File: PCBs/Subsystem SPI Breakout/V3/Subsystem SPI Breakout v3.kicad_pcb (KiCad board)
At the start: 2 copper layers, 91.4 x 53.3 mm, 33 parts

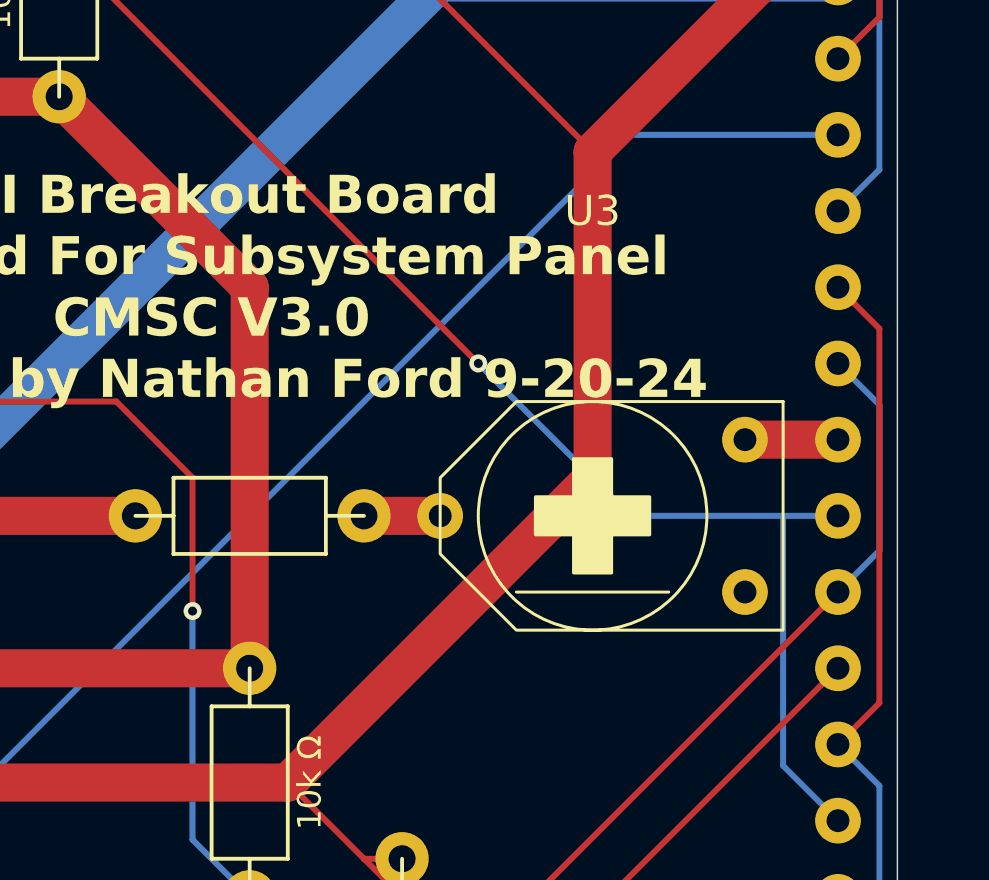
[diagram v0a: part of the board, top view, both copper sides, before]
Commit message: Fixed some labels on the silkscreen
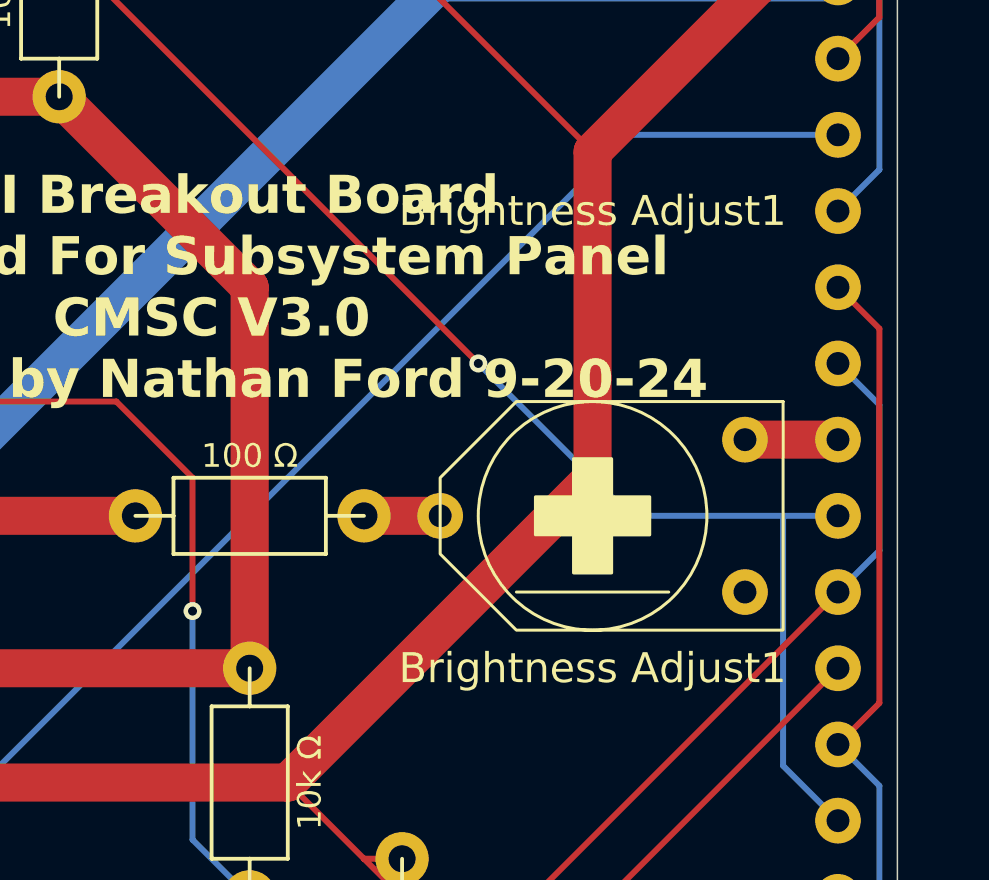
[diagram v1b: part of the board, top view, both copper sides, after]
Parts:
- Brightness Adjust1: renamed from U3
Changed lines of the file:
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@@
 	(net 19 "/CS_TOUCH_3V3")
 	(net 20 "/RESET_3V3")
-	(net 21 "Net-(R9-PadP$2)")
+	(net 21 "Net-(Brightness Adjust1-PadVout1)")
 	(net 22 "Net-(Amplifying Transistor1-B)")
 	(net 23 "Net-(Amplifying Transistor1-E)")
 	(net 24 "Net-(LS1-Pad2)")
 	(net 25 "Net-(U1-T_IRQ)")
-	(net 26 "Net-(U2-PadLED)")
-	(net 27 "unconnected-(U3-PadVout2)")
+	(net 26 "unconnected-(Brightness Adjust1-PadVout2)")
+	(net 27 "Net-(Brightness Adjust1-PadVin)")
 	(footprint "Subsystem Main:THROUGH_HOLE_RESISTOR"
 		(layer "F.Cu")
@@
 		(property "Value" "100 Ω"
 			(at 0 -2 0)
-			(layer "F.Fab")
+			(layer "F.SilkS")
 			(effects
 				(font
@@
 			(layers "*.Cu" "*.Mask")
 			(remove_unused_layers no)
-			(net 21 "Net-(R9-PadP$2)")
+			(net 27 "Net-(Brightness Adjust1-PadVin)")
 			(pinfunction "P$2")
 			(pintype "bidirectional")
@@
 		(layer "F.Cu")
 		(at 187.96 99.06)
-		(property "Reference" "U3"
+		(property "Reference" "Brightness Adjust1"
 			(at 0 -10.16 0)
 			(unlocked yes)
@@
 		)
 		(property "Value" "~"
-			(at 0 8.89 0)
+			(at 0 3.175 0)
 			(unlocked yes)
 			(layer "F.Fab")
@@
 		)
 		(fp_text user "${REFERENCE}"
-			(at 0 10.39 0)
+			(at 0 5.08 0)
 			(unlocked yes)
-			(layer "F.Fab")
+			(layer "F.SilkS")
 			(effects
 				(font
@@
 			(layers "*.Cu" "*.Mask")
 			(remove_unused_layers no)
-			(net 21 "Net-(R9-PadP$2)")
+			(net 27 "Net-(Brightness Adjust1-PadVin)")
 			(pintype "input")
 		)
@@
 			(layers "*.Cu" "*.Mask")
 			(remove_unused_layers no)
-			(net 26 "Net-(U2-PadLED)")
+			(net 21 "Net-(Brightness Adjust1-PadVout1)")
 			(pintype "output")
 		)
@@
 			(layers "*.Cu" "*.Mask")
 			(remove_unused_layers no)
-			(net 27 "unconnected-(U3-PadVout2)")
+			(net 26 "unconnected-(Brightness Adjust1-PadVout2)")
 			(pintype "output")
 		)
@@
 			(layers "*.Cu" "*.Mask")
 			(remove_unused_layers no)
-			(net 26 "Net-(U2-PadLED)")
+			(net 21 "Net-(Brightness Adjust1-PadVout1)")
 			(pinfunction "LED")
 			(pintype "input")
@@
 	)
 	(segment
-		(start 180.34 99.06)
-		(end 182.88 99.06)
+		(start 193.04 96.52)
+		(end 196.14 96.52)
 		(width 1.27)
 		(layer "F.Cu")
@@
 	)
 	(segment
-		(start 193.04 96.52)
-		(end 196.14 96.52)
+		(start 180.34 99.06)
+		(end 182.88 99.06)
 		(width 1.27)
 		(layer "F.Cu")
-		(net 26)
+		(net 27)
 	)
 )
